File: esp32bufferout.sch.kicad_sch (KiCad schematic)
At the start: 20 parts, among them U10 TL072, U11 TL072, U12 TL072

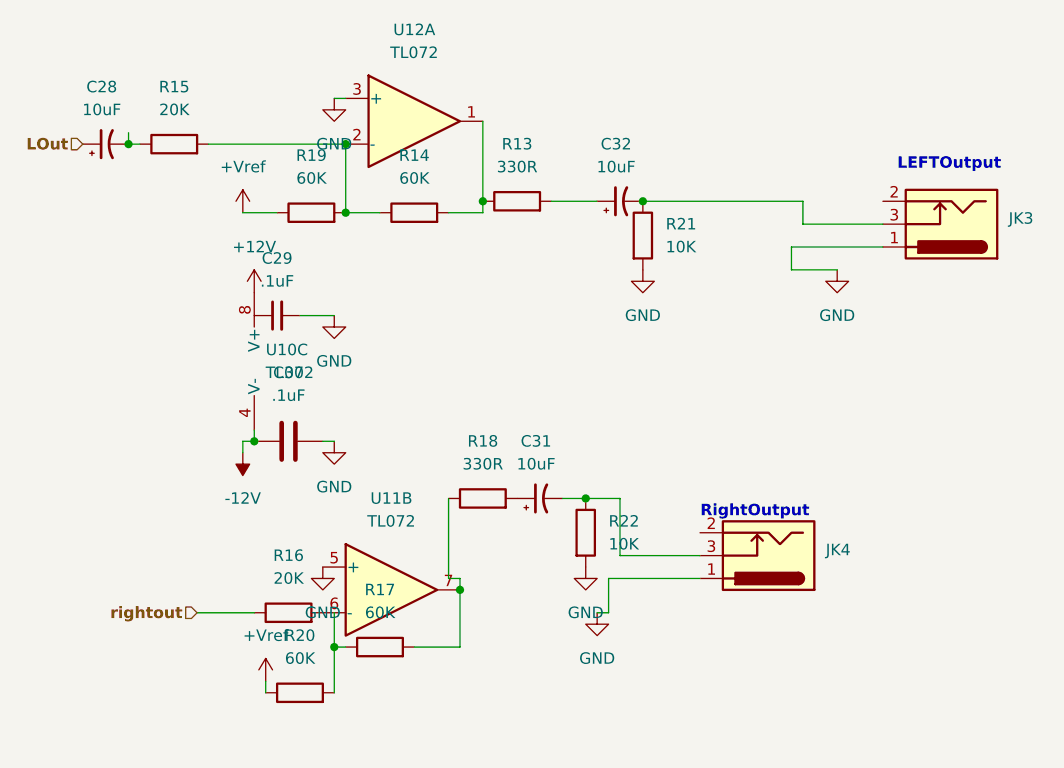
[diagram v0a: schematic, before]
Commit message: updated common lib symbols and footprint models
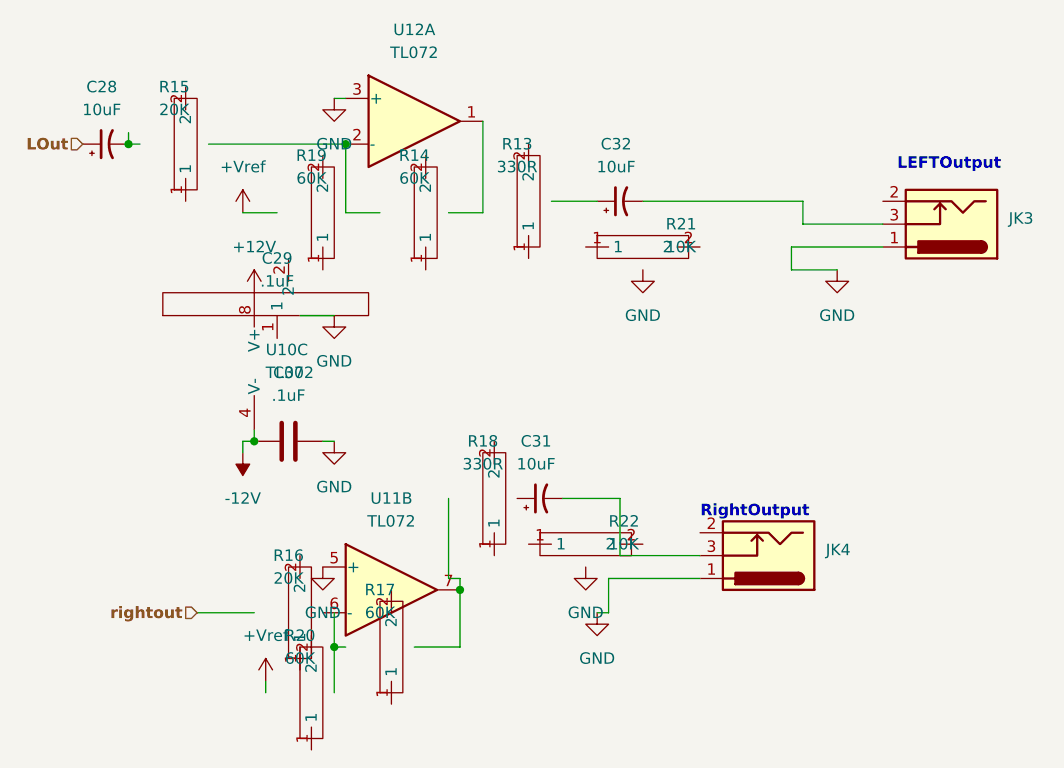
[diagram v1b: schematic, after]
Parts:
- C29: footprint Capacitor_SMD:C_0201_0603Metric -> commonfootprint:Ceramic0603; symbol Device:C_Small -> common:CerCap
- R13, R18: footprint Resistor_SMD:R_0201_0603Metric -> commonfootprint:Modcan0603; symbol Device:R -> common:R
- R14, R15, R16, R17, R19, R20, R21, R22: footprint (none) -> commonfootprint:Modcan0603; symbol Device:R -> common:R
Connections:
- net +Vref: no longer R19.1, R20.1
- net GND: no longer C29.2, R21.2, R22.2
- net rightout: no longer R16.1
- net at C28.2: no longer R15.1
- net at R13.2: no longer C32.1
- net at C31.2, JK4.3: no longer R22.1
- net at R20.2: no longer R17.1
- net at C32.2, JK3.3: no longer R21.1
- net at C31.1: no longer R18.2
- net at R16.2: no longer U11.6 (-)
- now unconnected: R13.1, R14.1, R14.2, R15.2, R17.2, R18.1, R19.2, U11.7, U12.1, U12.2 (-)
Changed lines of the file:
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@@
-	)
-	(junction
-		(at 93.98 48.26)
-		(diameter 0)
-		(color 0 0 0 0)
-	)
-	(junction
-		(at 87.63 81.28)
-		(diameter 0)
-		(color 0 0 0 0)
-	)
-	(junction
-		(at 76.2 48.26)
-		(diameter 0)
-		(color 0 0 0 0)
 	)
 	(junction
@@
 		(color 0 0 0 0)
 	)
-	(junction
-		(at 60.96 49.53)
-		(diameter 0)
-		(color 0 0 0 0)
-	)
 	(wire
 		(pts
@@
 	(wire
 		(pts
-			(xy 76.2 39.37) (xy 76.2 48.26)
-		)
-		(stroke
-			(width 0)
-			(type default)
-		)
-	)
-	(wire
-		(pts
 			(xy 120.65 50.8) (xy 111.76 50.8)
 		)
@@
 	(wire
 		(pts
-			(xy 91.44 81.28) (xy 87.63 81.28)
-		)
-		(stroke
-			(width 0)
-			(type default)
-		)
-	)
-	(wire
-		(pts
 			(xy 49.53 74.93) (xy 50.8 74.93)
 		)
@@
 	(wire
 		(pts
-			(xy 76.2 48.26) (xy 76.2 49.53)
+			(xy 76.2 39.37) (xy 76.2 49.53)
 		)
 		(stroke
@@
 	(wire
 		(pts
-			(xy 87.63 81.28) (xy 85.09 81.28)
+			(xy 85.09 81.28) (xy 91.44 81.28)
 		)
 		(stroke
@@
 	)
 	(symbol
-		(lib_id "Device:R")
+		(lib_id "common:R")
 		(at 57.15 49.53 90)
 		(unit 1)
@@
 			)
 		)
-		(property "Footprint" ""
+		(property "Footprint" "commonfootprint:Modcan0603"
 			(at 57.15 51.308 90)
 			(effects
@@
 	)
 	(symbol
-		(lib_id "Device:R")
+		(lib_id "common:R")
 		(at 80.01 48.26 90)
 		(unit 1)
@@
 			)
 		)
-		(property "Footprint" "Resistor_SMD:R_0201_0603Metric"
+		(property "Footprint" "commonfootprint:Modcan0603"
 			(at 80.01 50.038 90)
 			(effects
@@
 	)
 	(symbol
-		(lib_id "Device:R")
+		(lib_id "common:R")
 		(at 55.88 102.87 90)
 		(unit 1)
@@
 			)
 		)
-		(property "Footprint" ""
+		(property "Footprint" "commonfootprint:Modcan0603"
 			(at 55.88 104.648 90)
 			(effects
@@
 	)
 	(symbol
-		(lib_id "Device:R")
+		(lib_id "common:R")
 		(at 68.58 49.53 90)
 		(unit 1)
@@
 			)
 		)
-		(property "Footprint" ""
+		(property "Footprint" "commonfootprint:Modcan0603"
 			(at 68.58 51.308 90)
 			(effects
@@
 	)
 	(symbol
-		(lib_id "Device:R")
+		(lib_id "common:R")
 		(at 64.77 97.79 90)
 		(unit 1)
@@
 			)
 		)
-		(property "Footprint" ""
+		(property "Footprint" "commonfootprint:Modcan0603"
 			(at 64.77 99.568 90)
 			(effects
@@
 	)
 	(symbol
-		(lib_id "Device:C_Small")
+		(lib_id "common:CerCap")
 		(at 53.34 60.96 90)
 		(unit 1)
@@
 			)
 		)
-		(property "Footprint" "Capacitor_SMD:C_0201_0603Metric"
+		(property "Footprint" "commonfootprint:Ceramic0603"
 			(at 53.34 60.96 0)
 			(effects
@@
 	)
 	(symbol
-		(lib_id "Device:R")
+		(lib_id "common:R")
 		(at 41.91 41.91 90)
 		(unit 1)
@@
 			)
 		)
-		(property "Footprint" ""
+		(property "Footprint" "commonfootprint:Modcan0603"
 			(at 41.91 43.688 90)
 			(effects
@@
 	)
 	(symbol
-		(lib_id "Device:R")
+		(lib_id "common:R")
 		(at 54.61 93.98 90)
 		(unit 1)
@@
 			)
 		)
-		(property "Footprint" ""
+		(property "Footprint" "commonfootprint:Modcan0603"
 			(at 54.61 95.758 90)
 			(effects
@@
 	)
 	(symbol
-		(lib_id "Device:R")
+		(lib_id "common:R")
 		(at 76.2 81.28 90)
 		(unit 1)
@@
 			)
 		)
-		(property "Footprint" "Resistor_SMD:R_0201_0603Metric"
+		(property "Footprint" "commonfootprint:Modcan0603"
 			(at 76.2 83.058 90)
 			(effects
@@
 	)
 	(symbol
-		(lib_id "Device:R")
+		(lib_id "common:R")
 		(at 87.63 85.09 0)
 		(unit 1)
@@
 			)
 		)
-		(property "Footprint" ""
+		(property "Footprint" "commonfootprint:Modcan0603"
 			(at 85.852 85.09 90)
 			(effects
@@
 	)
 	(symbol
-		(lib_id "Device:R")
+		(lib_id "common:R")
 		(at 93.98 52.07 0)
 		(unit 1)
@@
 			)
 		)
-		(property "Footprint" ""
+		(property "Footprint" "commonfootprint:Modcan0603"
 			(at 92.202 52.07 90)
 			(effects

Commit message: updated a few caps
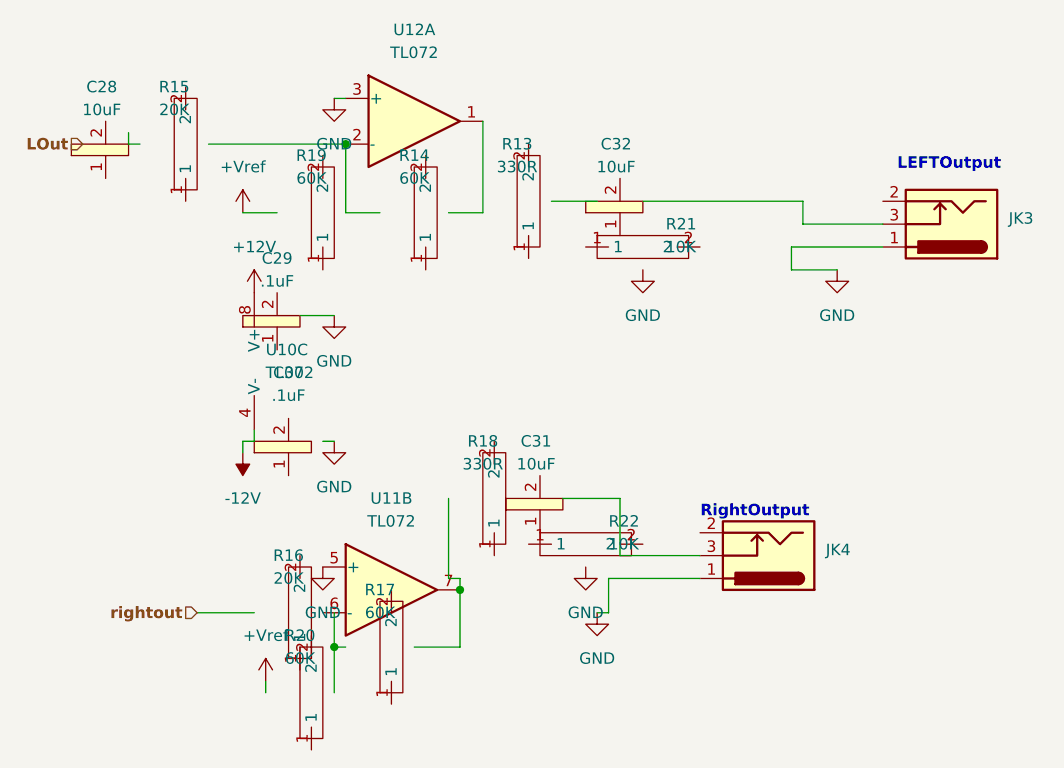
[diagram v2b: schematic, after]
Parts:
- C28, C31, C32: footprint Capacitor_SMD:CP_Elec_3x5.3 -> commonfootprint:Ceramic0603; symbol Device:C_Polarized_Small_US -> common:CerCap
- C30: footprint (none) -> commonfootprint:Ceramic0603; symbol Device:C -> common:CerCap
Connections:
- net -12V: no longer C30.1
- net GND: no longer C30.2
- net LOut: no longer C28.1
- net at JK4.3: no longer C31.2
- net at C32.2: no longer JK3.3
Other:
- moved on the sheet: C28, C31, C32
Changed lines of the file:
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@@
-	)
-	(junction
-		(at 36.83 41.91)
-		(diameter 0)
-		(color 0 0 0 0)
 	)
 	(junction
@@
 	(junction
 		(at 60.96 41.91)
-		(diameter 0)
-		(color 0 0 0 0)
-	)
-	(junction
-		(at 50.8 74.93)
 		(diameter 0)
 		(color 0 0 0 0)
@@
 	)
 	(symbol
-		(lib_id "Device:C_Polarized_Small_US")
+		(lib_id "common:CerCap")
 		(at 34.29 41.91 90)
 		(unit 1)
@@
 			)
 		)
-		(property "Footprint" "Capacitor_SMD:CP_Elec_3x5.3"
+		(property "Footprint" "commonfootprint:Ceramic0603"
 			(at 34.29 41.91 0)
 			(effects
@@
 	)
 	(symbol
-		(lib_id "Device:C")
+		(lib_id "common:CerCap")
 		(at 54.61 74.93 90)
 		(unit 1)
@@
 			)
 		)
-		(property "Footprint" ""
+		(property "Footprint" "commonfootprint:Ceramic0603"
 			(at 58.42 73.9648 0)
 			(effects
@@
 	)
 	(symbol
-		(lib_id "Device:C_Polarized_Small_US")
+		(lib_id "common:CerCap")
 		(at 91.44 48.26 90)
 		(unit 1)
@@
 			)
 		)
-		(property "Footprint" "Capacitor_SMD:CP_Elec_3x5.3"
+		(property "Footprint" "commonfootprint:Ceramic0603"
 			(at 91.44 48.26 0)
 			(effects
@@
 	)
 	(symbol
-		(lib_id "Device:C_Polarized_Small_US")
+		(lib_id "common:CerCap")
 		(at 82.55 81.28 90)
 		(unit 1)
@@
 			)
 		)
-		(property "Footprint" "Capacitor_SMD:CP_Elec_3x5.3"
+		(property "Footprint" "commonfootprint:Ceramic0603"
 			(at 82.55 81.28 0)
 			(effects
